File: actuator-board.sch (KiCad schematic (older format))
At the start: 28 parts, among them U1 STM32F302K8U6, U2 MCP1703, U3 MAX3051, X1 16MHz 10ppm

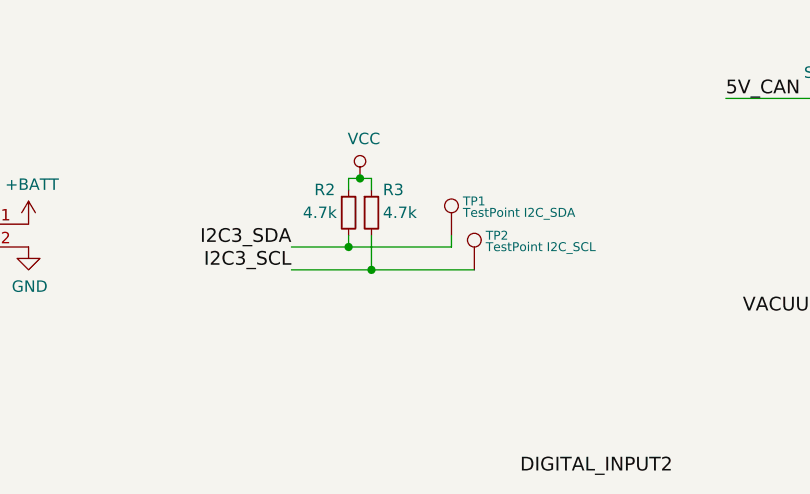
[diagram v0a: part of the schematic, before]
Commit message: Work on footprint assignment
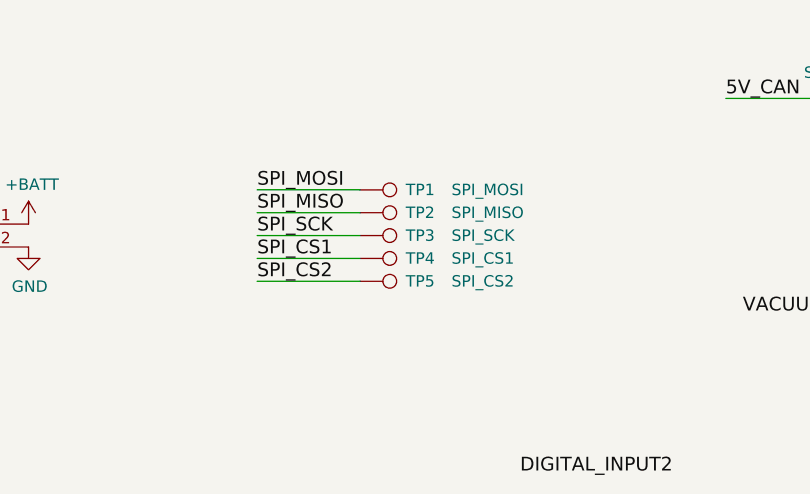
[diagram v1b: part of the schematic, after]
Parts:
- removed R2, R3: 4.7k, symbol Device:R_Small
- added TP3: SPI_SCK, symbol Connector:TestPoint
- added TP4: SPI_CS1, symbol Connector:TestPoint
- added TP5: SPI_CS2, symbol Connector:TestPoint
- CONN1: footprint Connector_Molex:Molex_PicoBlade_53048-1410_1x07_P1.25mm_Horizontal -> Connector_Molex:Molex_PicoBlade_53048-0710_1x07_P1.25mm_Horizontal
- TP1: value TestPoint I2C_SDA -> SPI_MOSI
- TP2: value TestPoint I2C_SCL -> SPI_MISO
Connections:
- net I2C3_SCL is gone; now on net SPI_MISO: TP2.1
- net I2C3_SDA is gone; now on net SPI_MOSI: TP1.1
- net SPI_CS1: now also TP4.1
- net SPI_CS2: now also TP5.1
- net SPI_SCK: now also TP3.1
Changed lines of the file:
@@
 F 0 "CONN1" H 1400 2250 50  0000 C CNN
 F 1 "SWD/DEBUG" H 1400 1350 50  0000 C CNN
-F 2 "Connector_Molex:Molex_PicoBlade_53048-1410_1x07_P1.25mm_Horizontal" H 1400 1750 50  0001 C CNN
+F 2 "Connector_Molex:Molex_PicoBlade_53048-0710_1x07_P1.25mm_Horizontal" H 1400 1750 50  0001 C CNN
 F 3 "DOCUMENTATION" H 1400 1750 50  0001 C CNN
 	1    1400 1800
@@
 Wire Wire Line
 	5350 3600 5450 3600
-Text Label 6200 2650 0    60   ~ 0
-DIGITAL_INPUT2
 Text Label 8100 3100 2    50   ~ 0
 DIGITAL_INPUT2
@@
 Wire Wire Line
 	8100 3100 8250 3100
-$Comp
-L Device:R_Small R2
-U 1 1 5E2B5517
-P 5450 1500
-F 0 "R2" H 5300 1600 50  0000 L CNN
-F 1 "4.7k" H 5250 1500 50  0000 L CNN
-F 2 "" H 5450 1500 50  0001 C CNN
-F 3 "~" H 5450 1500 50  0001 C CNN
-	1    5450 1500
-	1    0    0    -1
-$EndComp
-$Comp
-L Device:R_Small R3
-U 1 1 5E2B5518
-P 5550 1500
-F 0 "R3" H 5600 1600 50  0000 L CNN
-F 1 "4.7k" H 5600 1500 50  0000 L CNN
-F 2 "" H 5550 1500 50  0001 C CNN
-F 3 "~" H 5550 1500 50  0001 C CNN
-	1    5550 1500
-	1    0    0    -1
-$EndComp
-$Comp
-L power:VCC #PWR013
-U 1 1 5E2B5516
-P 5500 1350
-F 0 "#PWR013" H 5500 1200 50  0001 C CNN
-F 1 "VCC" H 5517 1523 50  0000 C CNN
-F 2 "" H 5500 1350 50  0001 C CNN
-F 3 "" H 5500 1350 50  0001 C CNN
-	1    5500 1350
-	1    0    0    -1
-$EndComp
-$Comp
-L Connector:TestPoint TP?
-U 1 1 5E516367
-P 5900 1600
-AR Path="/5E1FAFCF/5E516367" Ref="TP?"  Part="1"
-AR Path="/5E516367" Ref="TP1"  Part="1"
-F 0 "TP1" H 5950 1750 39  0000 L CNN
-F 1 "TestPoint I2C_SDA" H 5950 1700 39  0000 L CNN
-F 2 "" H 6100 1600 50  0001 C CNN
-F 3 "~" H 6100 1600 50  0001 C CNN
-	1    5900 1600
-	1    0    0    -1
-$EndComp
-$Comp
-L Connector:TestPoint TP?
-U 1 1 5E516361
-P 6000 1750
-AR Path="/5E1FAFCF/5E516361" Ref="TP?"  Part="1"
-AR Path="/5E516361" Ref="TP2"  Part="1"
-F 0 "TP2" H 6050 1900 39  0000 L CNN
-F 1 "TestPoint I2C_SCL" H 6050 1850 39  0000 L CNN
-F 2 "" H 6200 1750 50  0001 C CNN
-F 3 "~" H 6200 1750 50  0001 C CNN
-	1    6000 1750
-	1    0    0    -1
-$EndComp
-Text Label 5200 1750 2    60   ~ 0
-I2C3_SCL
-Text Label 5200 1650 2    60   ~ 0
-I2C3_SDA
-Wire Wire Line
-	5200 1750 5550 1750
-Wire Wire Line
-	5200 1650 5450 1650
-Wire Wire Line
-	5450 1600 5450 1650
-Connection ~ 5450 1650
-Wire Wire Line
-	5450 1650 5900 1650
-Wire Wire Line
-	5550 1600 5550 1750
-Connection ~ 5550 1750
-Wire Wire Line
-	5550 1750 6000 1750
-Wire Wire Line
-	5550 1350 5500 1350
-Connection ~ 5500 1350
-Wire Wire Line
-	5500 1350 5450 1350
-Wire Wire Line
-	5450 1350 5450 1400
-Wire Wire Line
-	5550 1350 5550 1400
-Wire Wire Line
-	5900 1600 5900 1650
 Text Label 6350 5400 0    60   ~ 0
 DIGITAL_INPUT1
@@
 Wire Wire Line
 	8100 1950 8200 1950
+$Comp
+L Connector:TestPoint TP?
+U 1 1 5E3DC2A8
+P 5500 1600
+AR Path="/5E1FAFCF/5E3DC2A8" Ref="TP?"  Part="1"
+AR Path="/5E3DC2A8" Ref="TP3"  Part="1"
+F 0 "TP3" V 5500 1800 50  0000 L CNN
+F 1 "SPI_SCK" V 5500 2000 50  0000 L CNN
+F 2 "" H 5700 1600 50  0001 C CNN
+F 3 "~" H 5700 1600 50  0001 C CNN
+	1    5500 1600
+	0    1    1    0
+$EndComp
+Text Label 5050 1800 0    60   ~ 0
+SPI_CS2
+Text Label 5050 1700 0    60   ~ 0
+SPI_CS1
+Text Label 5050 1600 0    60   ~ 0
+SPI_SCK
+Text Label 5050 1500 0    60   ~ 0
+SPI_MISO
+Text Label 5050 1400 0    60   ~ 0
+SPI_MOSI
+$Comp
+L Connector:TestPoint TP?
+U 1 1 5E3FB967
+P 5500 1400
+AR Path="/5E1FAFCF/5E3FB967" Ref="TP?"  Part="1"
+AR Path="/5E3FB967" Ref="TP1"  Part="1"
+F 0 "TP1" V 5500 1600 50  0000 L CNN
+F 1 "SPI_MOSI" V 5500 1800 50  0000 L CNN
+F 2 "" H 5700 1400 50  0001 C CNN
+F 3 "~" H 5700 1400 50  0001 C CNN
+	1    5500 1400
+	0    1    1    0
+$EndComp
+$Comp
+L Connector:TestPoint TP?
+U 1 1 5E401584
+P 5500 1500
+AR Path="/5E1FAFCF/5E401584" Ref="TP?"  Part="1"
+AR Path="/5E401584" Ref="TP2"  Part="1"
+F 0 "TP2" V 5500 1700 50  0000 L CNN
+F 1 "SPI_MISO" V 5500 1900 50  0000 L CNN
+F 2 "" H 5700 1500 50  0001 C CNN
+F 3 "~" H 5700 1500 50  0001 C CNN
+	1    5500 1500
+	0    1    1    0
+$EndComp
+$Comp
+L Connector:TestPoint TP?
+U 1 1 5E401823
+P 5500 1700
+AR Path="/5E1FAFCF/5E401823" Ref="TP?"  Part="1"
+AR Path="/5E401823" Ref="TP4"  Part="1"
+F 0 "TP4" V 5500 1900 50  0000 L CNN
+F 1 "SPI_CS1" V 5500 2100 50  0000 L CNN
+F 2 "" H 5700 1700 50  0001 C CNN
+F 3 "~" H 5700 1700 50  0001 C CNN
+	1    5500 1700
+	0    1    1    0
+$EndComp
+$Comp
+L Connector:TestPoint TP?
+U 1 1 5E401A3D
+P 5500 1800
+AR Path="/5E1FAFCF/5E401A3D" Ref="TP?"  Part="1"
+AR Path="/5E401A3D" Ref="TP5"  Part="1"
+F 0 "TP5" V 5500 2000 50  0000 L CNN
+F 1 "SPI_CS2" V 5500 2200 50  0000 L CNN
+F 2 "" H 5700 1800 50  0001 C CNN
+F 3 "~" H 5700 1800 50  0001 C CNN
+	1    5500 1800
+	0    1    1    0
+$EndComp
+Wire Wire Line
+	5050 1400 5500 1400
+Wire Wire Line
+	5050 1500 5500 1500
+Wire Wire Line
+	5050 1600 5500 1600
+Wire Wire Line
+	5050 1700 5500 1700
+Wire Wire Line
+	5500 1800 5050 1800
+Text Label 6200 2650 0    60   ~ 0
+DIGITAL_INPUT2
 $EndSCHEMATC

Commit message: Review update
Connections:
- net 5V_CAN renamed +5V
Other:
- note added: "Features:\n2x pump half bridge\n2x solenoid half bridge\n2x vacuum sensor SPI\n2 Servo PWM\n2 analog input\n1 digital input"
- note added: "Note:\nDIGITAL_INPUT1\nshared with\nUART1RX"
- note removed: "2x pump half bridge\n2x solenoid half bridge\n2x vacuum sensor I2C\n1-2 Servo PWM\n1-2 analog input\n1-2 digital input"
- moved on the sheet: R4, R5
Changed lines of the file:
@@
 Sheet 1 3
 Title "Actuator board"
-Date "2020-01-25"
-Rev "A.3"
+Date "2020-02-12"
+Rev "A.4"
 Comp "Club Vaudois de Robotique Autonome"
 Comment1 "Salah Missri"
@@
 	1    0    0    -1
 $EndComp
-Text Label 10100 4800 2    60   ~ 0
-5V_CAN
-Text Label 10100 5750 2    60   ~ 0
-5V_CAN
 $Comp
 L power:GND #PWR021
@@
 	5350 3800 5450 3800
 Wire Wire Line
-	5450 4100 5350 4100
-Wire Wire Line
-	5450 4000 5350 4000
+	5800 4100 5350 4100
+Wire Wire Line
+	5800 4000 5350 4000
 Wire Wire Line
 	1750 2000 1800 2000
@@
 	9950 4900 10150 4900
 Wire Wire Line
-	10100 4800 10150 4800
-Wire Wire Line
-	10100 5750 10150 5750
+	9950 4800 10150 4800
+Wire Wire Line
+	9950 5750 10150 5750
 Wire Wire Line
 	3100 4000 3350 4000
@@
 Wire Wire Line
 	5450 3200 5350 3200
-Text Label 5700 4000 0    60   ~ 0
+Text Label 6150 4000 0    60   ~ 0
 SERVO1
-Text Label 5700 4100 0    60   ~ 0
+Text Label 6150 4100 0    60   ~ 0
 SERVO2
 Text Label 5450 3800 0    60   ~ 0
@@
 Text Label 5450 3200 0    60   ~ 0
 ANALOG2
-Text Label 5450 3100 0    60   ~ 0
-ANALOG1
 Wire Wire Line
 	8100 5550 8100 5650
@@
 Wire Wire Line
 	8000 5650 8100 5650
-Text Notes 2350 6300 0    60   ~ 0
-2x pump half bridge\n2x solenoid half bridge\n2x vacuum sensor I2C\n1-2 Servo PWM\n1-2 analog input\n1-2 digital input
+Text Notes 1150 7400 0    60   ~ 0
+Features:\n2x pump half bridge\n2x solenoid half bridge\n2x vacuum sensor SPI\n2 Servo PWM\n2 analog input\n1 digital input
 Wire Wire Line
 	3400 3100 3550 3100
@@
 	1    0    0    -1
 $EndComp
-Text Label 7100 1000 0    60   ~ 0
-5V_CAN
 $Comp
 L Device:C C10
@@
 Connection ~ 9450 1000
 Wire Wire Line
-	7100 1000 7700 1000
+	7250 1000 7700 1000
 $Comp
 L Device:D_Schottky_Small D2
@@
 Text Label 5450 3500 0    60   ~ 0
 VACUUM_SENS_RESET
-Text Label 8100 3000 2    50   ~ 0
+Text Label 8100 3000 2    60   ~ 0
 DIGITAL_INPUT1
 Wire Wire Line
@@
 	1750 1500 2150 1500
 $Sheet
-S 8250 1850 1450 1350
+S 8250 1850 1450 1250
 U 5E1FAFCF
 F0 "Sensors" 50
@@
 F4 "ANALOG_SENS_IN2" I L 8250 2850 50
 F5 "DIGITAL_IN1" I L 8250 3000 50
-F6 "DIGITAL_IN2" I L 8250 3100 50
-F7 "VACUUM_SENS2_RESET" I L 8250 2050 50
-F8 "SPI_SCK" I L 8250 2200 50
-F9 "SPI_MOSI" I L 8250 2300 50
-F10 "SPI_MISO" I L 8250 2400 50
-F11 "VACUUM_SENS1_CS" I L 8250 2500 50
-F12 "VACUUM_SENS2_CS" I L 8250 2600 50
+F6 "VACUUM_SENS2_RESET" I L 8250 2050 50
+F7 "SPI_SCK" I L 8250 2200 50
+F8 "SPI_MOSI" I L 8250 2300 50
+F9 "SPI_MISO" I L 8250 2400 50
+F10 "VACUUM_SENS1_CS" I L 8250 2500 50
+F11 "VACUUM_SENS2_CS" I L 8250 2600 50
 $EndSheet
 $Sheet
@@
 Wire Wire Line
 	5350 3600 5450 3600
-Text Label 8100 3100 2    50   ~ 0
-DIGITAL_INPUT2
 Wire Wire Line
 	5350 5100 5450 5100
@@
 L Device:R_Small R4
 U 1 1 5E2FD4D2
-P 5550 4000
-F 0 "R4" V 5525 3850 39  0000 C CNN
-F 1 "330" V 5550 4000 39  0000 C CNN
-F 2 "" H 5550 4000 50  0001 C CNN
-F 3 "~" H 5550 4000 50  0001 C CNN
-	1    5550 4000
+P 5900 4000
+F 0 "R4" V 5875 3850 39  0000 C CNN
+F 1 "330" V 5900 4000 39  0000 C CNN
+F 2 "" H 5900 4000 50  0001 C CNN
+F 3 "~" H 5900 4000 50  0001 C CNN
+	1    5900 4000
 	0    1    1    0
 $EndComp
 Wire Wire Line
-	5650 4000 5700 4000
+	6000 4000 6150 4000
 $Comp
 L Device:R_Small R5
 U 1 1 5E300459
-P 5550 4100
-F 0 "R5" V 5525 3950 39  0000 C CNN
-F 1 "330" V 5550 4100 39  0000 C CNN
-F 2 "" H 5550 4100 50  0001 C CNN
-F 3 "~" H 5550 4100 50  0001 C CNN
-	1    5550 4100
+P 5900 4100
+F 0 "R5" V 5875 3950 39  0000 C CNN
+F 1 "330" V 5900 4100 39  0000 C CNN
+F 2 "" H 5900 4100 50  0001 C CNN
+F 3 "~" H 5900 4100 50  0001 C CNN
+	1    5900 4100
 	0    1    1    0
 $EndComp
 Wire Wire Line
-	5650 4100 5700 4100
+	6000 4100 6150 4100
 Wire Wire Line
 	8100 3700 8250 3700
@@
 Wire Wire Line
 	8250 3000 8100 3000
-Wire Wire Line
-	8100 3100 8250 3100
 Text Label 6350 5400 0    60   ~ 0
 DIGITAL_INPUT1
@@
 Wire Wire Line
 	5500 1800 5050 1800
-Text Label 6200 2650 0    60   ~ 0
-DIGITAL_INPUT2
+Text Notes 6450 5200 0    60   ~ 0
+Note:\nDIGITAL_INPUT1\nshared with\nUART1RX
+$Comp
+L power:+5V #PWR0106
+U 1 1 5E44C5DA
+P 9950 4800
+F 0 "#PWR0106" H 9950 4650 50  0001 C CNN
+F 1 "+5V" H 9965 4973 50  0000 C CNN
+F 2 "" H 9950 4800 50  0001 C CNN
+F 3 "" H 9950 4800 50  0001 C CNN
+	1    9950 4800
+	1    0    0    -1
+$EndComp
+$Comp
+L power:+5V #PWR0107
+U 1 1 5E4595E8
+P 9950 5750
+F 0 "#PWR0107" H 9950 5600 50  0001 C CNN
+F 1 "+5V" H 9965 5923 50  0000 C CNN
+F 2 "" H 9950 5750 50  0001 C CNN
+F 3 "" H 9950 5750 50  0001 C CNN
+	1    9950 5750
+	1    0    0    -1
+$EndComp
+$Comp
+L power:+5V #PWR0108
+U 1 1 5E459C00
+P 7250 1000
+F 0 "#PWR0108" H 7250 850 50  0001 C CNN
+F 1 "+5V" H 7265 1173 50  0000 C CNN
+F 2 "" H 7250 1000 50  0001 C CNN
+F 3 "" H 7250 1000 50  0001 C CNN
+	1    7250 1000
+	1    0    0    -1
+$EndComp
+Text Label 5450 3100 0    60   ~ 0
+ANALOG1
 $EndSCHEMATC

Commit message: Input range note, rough footprint assignment
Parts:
- CONN2: footprint MODULE -> Connector_PinHeader_2.54mm:PinHeader_1x02_P2.54mm_Vertical
- R1: footprint Resistor_SMD:R_0402_1005Metric -> Resistor_SMD:R_0603_1608Metric
- R4, R5, R6: footprint (none) -> Resistor_SMD:R_0603_1608Metric
- TP1, TP2, TP3, TP4, TP5: footprint (none) -> TestPoint:TestPoint_Pad_D1.0mm
- U1: footprint Housings_DFN_QFN:QFN-32-1EP_5x5mm_Pitch0.5mm -> Package_DFN_QFN:QFN-32-1EP_5x5mm_P0.5mm_EP3.45x3.45mm
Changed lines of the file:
@@
 F 0 "CONN2" H 3650 1400 50  0000 C CNN
 F 1 "BATTERY" H 3650 1800 50  0000 C CNN
-F 2 "MODULE" H 3950 1600 50  0001 C CNN
+F 2 "Connector_PinHeader_2.54mm:PinHeader_1x02_P2.54mm_Vertical" H 3950 1600 50  0001 C CNN
 F 3 "DOCUMENTATION" H 3950 1600 50  0001 C CNN
 	1    3700 1600
@@
 F 0 "U1" H 5000 6000 60  0000 C CNN
 F 1 "STM32F302K8U6" H 4500 6000 60  0000 C CNN
-F 2 "Housings_DFN_QFN:QFN-32-1EP_5x5mm_Pitch0.5mm" H 4600 3950 60  0001 C CNN
+F 2 "Package_DFN_QFN:QFN-32-1EP_5x5mm_P0.5mm_EP3.45x3.45mm" H 4600 3950 60  0001 C CNN
 F 3 "DOCUMENTATION" H 4600 3950 60  0001 C CNN
 F 4 "497-14700-ND" H 4450 6100 50  0000 C CNN "Digikey"
@@
 F 0 "R1" V 1705 4325 50  0000 C CNN
 F 1 "510" V 1625 4325 50  0000 C CNN
-F 2 "Resistor_SMD:R_0402_1005Metric" V 1555 4325 50  0001 C CNN
+F 2 "Resistor_SMD:R_0603_1608Metric" V 1555 4325 50  0001 C CNN
 F 3 "" H 1625 4325 50  0000 C CNN
 	1    1625 4325
@@
 F 0 "R4" V 5875 3850 39  0000 C CNN
 F 1 "330" V 5900 4000 39  0000 C CNN
-F 2 "" H 5900 4000 50  0001 C CNN
+F 2 "Resistor_SMD:R_0603_1608Metric" H 5900 4000 50  0001 C CNN
 F 3 "~" H 5900 4000 50  0001 C CNN
 	1    5900 4000
@@
 F 0 "R5" V 5875 3950 39  0000 C CNN
 F 1 "330" V 5900 4100 39  0000 C CNN
-F 2 "" H 5900 4100 50  0001 C CNN
+F 2 "Resistor_SMD:R_0603_1608Metric" H 5900 4100 50  0001 C CNN
 F 3 "~" H 5900 4100 50  0001 C CNN
 	1    5900 4100
@@
 F 0 "R6" V 6075 5250 39  0000 C CNN
 F 1 "330" V 6100 5400 39  0000 C CNN
-F 2 "" H 6100 5400 50  0001 C CNN
+F 2 "Resistor_SMD:R_0603_1608Metric" H 6100 5400 50  0001 C CNN
 F 3 "~" H 6100 5400 50  0001 C CNN
 	1    6100 5400
@@
 F 0 "TP3" V 5500 1800 50  0000 L CNN
 F 1 "SPI_SCK" V 5500 2000 50  0000 L CNN
-F 2 "" H 5700 1600 50  0001 C CNN
+F 2 "TestPoint:TestPoint_Pad_D1.0mm" H 5700 1600 50  0001 C CNN
 F 3 "~" H 5700 1600 50  0001 C CNN
 	1    5500 1600
@@
 F 0 "TP1" V 5500 1600 50  0000 L CNN
 F 1 "SPI_MOSI" V 5500 1800 50  0000 L CNN
-F 2 "" H 5700 1400 50  0001 C CNN
+F 2 "TestPoint:TestPoint_Pad_D1.0mm" H 5700 1400 50  0001 C CNN
 F 3 "~" H 5700 1400 50  0001 C CNN
 	1    5500 1400
@@
 F 0 "TP2" V 5500 1700 50  0000 L CNN
 F 1 "SPI_MISO" V 5500 1900 50  0000 L CNN
-F 2 "" H 5700 1500 50  0001 C CNN
+F 2 "TestPoint:TestPoint_Pad_D1.0mm" H 5700 1500 50  0001 C CNN
 F 3 "~" H 5700 1500 50  0001 C CNN
 	1    5500 1500
@@
 F 0 "TP4" V 5500 1900 50  0000 L CNN
 F 1 "SPI_CS1" V 5500 2100 50  0000 L CNN
-F 2 "" H 5700 1700 50  0001 C CNN
+F 2 "TestPoint:TestPoint_Pad_D1.0mm" H 5700 1700 50  0001 C CNN
 F 3 "~" H 5700 1700 50  0001 C CNN
 	1    5500 1700
@@
 F 0 "TP5" V 5500 2000 50  0000 L CNN
 F 1 "SPI_CS2" V 5500 2200 50  0000 L CNN
-F 2 "" H 5700 1800 50  0001 C CNN
+F 2 "TestPoint:TestPoint_Pad_D1.0mm" H 5700 1800 50  0001 C CNN
 F 3 "~" H 5700 1800 50  0001 C CNN
 	1    5500 1800

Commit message: Upadate footprints, rough arrangement
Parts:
- added H1, H2, H3, H4: MountingHole, MountingHole:MountingHole_2.2mm_M2, symbol Mechanical:MountingHole
- C2, C3, C4, C5, C6, C7, C8: footprint Capacitor_SMD:C_0402_1005Metric -> Capacitor_SMD:C_0603_1608Metric
- CONN3, CONN4: footprint Connector_Molex:Molex_PicoBlade_53261-0471_1x04-1MP_P1.25mm_Horizontal -> Connector_Molex:Molex_PicoBlade_53398-0471_1x04-1MP_P1.25mm_Vertical
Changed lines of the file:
@@
 F 0 "CONN3" H 10500 5300 50  0000 C CNN
 F 1 "CAN" H 10500 4600 50  0000 C CNN
-F 2 "Connector_Molex:Molex_PicoBlade_53261-0471_1x04-1MP_P1.25mm_Horizontal" H 10750 4950 50  0001 C CNN
+F 2 "Connector_Molex:Molex_PicoBlade_53398-0471_1x04-1MP_P1.25mm_Vertical" H 10750 4950 50  0001 C CNN
 F 3 "DOCUMENTATION" H 10750 4950 50  0001 C CNN
 	1    10500 4950
@@
 F 0 "CONN4" H 10500 6250 50  0000 C CNN
 F 1 "CAN" H 10500 5550 50  0000 C CNN
-F 2 "Connector_Molex:Molex_PicoBlade_53261-0471_1x04-1MP_P1.25mm_Horizontal" H 10750 5900 50  0001 C CNN
+F 2 "Connector_Molex:Molex_PicoBlade_53398-0471_1x04-1MP_P1.25mm_Vertical" H 10750 5900 50  0001 C CNN
 F 3 "DOCUMENTATION" H 10750 5900 50  0001 C CNN
 	1    10500 5900
@@
 F 0 "C8" H 7475 5500 50  0000 L CNN
 F 1 "0.1uF" H 7475 5300 50  0000 L CNN
-F 2 "Capacitor_SMD:C_0402_1005Metric" H 7488 5250 50  0001 C CNN
+F 2 "Capacitor_SMD:C_0603_1608Metric" H 7488 5250 50  0001 C CNN
 F 3 "" H 7450 5400 50  0000 C CNN
 	1    7450 5400
@@
 F 0 "C5" H 3625 3900 50  0000 L CNN
 F 1 "0.1uF" H 3625 3700 50  0000 L CNN
-F 2 "Capacitor_SMD:C_0402_1005Metric" H 3638 3650 50  0001 C CNN
+F 2 "Capacitor_SMD:C_0603_1608Metric" H 3638 3650 50  0001 C CNN
 F 3 "" H 3600 3800 50  0000 C CNN
 	1    3600 3800
@@
 F 0 "C3" H 3525 4450 50  0000 L CNN
 F 1 "0.1uF" H 3525 4250 50  0000 L CNN
-F 2 "Capacitor_SMD:C_0402_1005Metric" H 3538 4200 50  0001 C CNN
+F 2 "Capacitor_SMD:C_0603_1608Metric" H 3538 4200 50  0001 C CNN
 F 3 "" H 3500 4350 50  0000 C CNN
 	1    3500 4350
@@
 F 0 "C2" H 3375 3900 50  0000 L CNN
 F 1 "0.1uF" H 3375 3700 50  0000 L CNN
-F 2 "Capacitor_SMD:C_0402_1005Metric" H 3388 3650 50  0001 C CNN
+F 2 "Capacitor_SMD:C_0603_1608Metric" H 3388 3650 50  0001 C CNN
 F 3 "" H 3350 3800 50  0000 C CNN
 	1    3350 3800
@@
 F 0 "C4" H 3575 3350 50  0000 L CNN
 F 1 "0.1uF" H 3575 3150 50  0000 L CNN
-F 2 "Capacitor_SMD:C_0402_1005Metric" H 3588 3100 50  0001 C CNN
+F 2 "Capacitor_SMD:C_0603_1608Metric" H 3588 3100 50  0001 C CNN
 F 3 "" H 3550 3250 50  0000 C CNN
 	1    3550 3250
@@
 F 0 "C6" H 5625 6100 50  0000 L CNN
 F 1 "10pF" H 5625 5900 50  0000 L CNN
-F 2 "Capacitor_SMD:C_0402_1005Metric" H 5638 5850 50  0001 C CNN
+F 2 "Capacitor_SMD:C_0603_1608Metric" H 5638 5850 50  0001 C CNN
 F 3 "" H 5600 6000 50  0000 C CNN
 	1    5600 6000
@@
 F 0 "C7" H 6325 6100 50  0000 L CNN
 F 1 "10pF" H 6325 5900 50  0000 L CNN
-F 2 "Capacitor_SMD:C_0402_1005Metric" H 6338 5850 50  0001 C CNN
+F 2 "Capacitor_SMD:C_0603_1608Metric" H 6338 5850 50  0001 C CNN
 F 3 "" H 6300 6000 50  0000 C CNN
 	1    6300 6000
@@
 Text Label 5450 3100 0    60   ~ 0
 ANALOG1
+$Comp
+L Mechanical:MountingHole H1
+U 1 1 5E4606C0
+P 3250 6800
+F 0 "H1" H 3350 6846 50  0000 L CNN
+F 1 "MountingHole" H 3350 6755 50  0000 L CNN
+F 2 "MountingHole:MountingHole_2.2mm_M2" H 3250 6800 50  0001 C CNN
+F 3 "~" H 3250 6800 50  0001 C CNN
+	1    3250 6800
+	1    0    0    -1
+$EndComp
+$Comp
+L Mechanical:MountingHole H2
+U 1 1 5E46075F
+P 3250 7000
+F 0 "H2" H 3350 7046 50  0000 L CNN
+F 1 "MountingHole" H 3350 6955 50  0000 L CNN
+F 2 "MountingHole:MountingHole_2.2mm_M2" H 3250 7000 50  0001 C CNN
+F 3 "~" H 3250 7000 50  0001 C CNN
+	1    3250 7000
+	1    0    0    -1
+$EndComp
+$Comp
+L Mechanical:MountingHole H3
+U 1 1 5E460FB2
+P 3250 7200
+F 0 "H3" H 3350 7246 50  0000 L CNN
+F 1 "MountingHole" H 3350 7155 50  0000 L CNN
+F 2 "MountingHole:MountingHole_2.2mm_M2" H 3250 7200 50  0001 C CNN
+F 3 "~" H 3250 7200 50  0001 C CNN
+	1    3250 7200
+	1    0    0    -1
+$EndComp
+$Comp
+L Mechanical:MountingHole H4
+U 1 1 5E4612D7
+P 3250 7400
+F 0 "H4" H 3350 7446 50  0000 L CNN
+F 1 "MountingHole" H 3350 7355 50  0000 L CNN
+F 2 "MountingHole:MountingHole_2.2mm_M2" H 3250 7400 50  0001 C CNN
+F 3 "~" H 3250 7400 50  0001 C CNN
+	1    3250 7400
+	1    0    0    -1
+$EndComp
 $EndSCHEMATC
